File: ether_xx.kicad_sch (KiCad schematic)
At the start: 17 parts, among them J1 RJ45_LED_Shielded, J2 RJ45_LED_Shielded, U2 LAN8710A, U3 LAN8710A

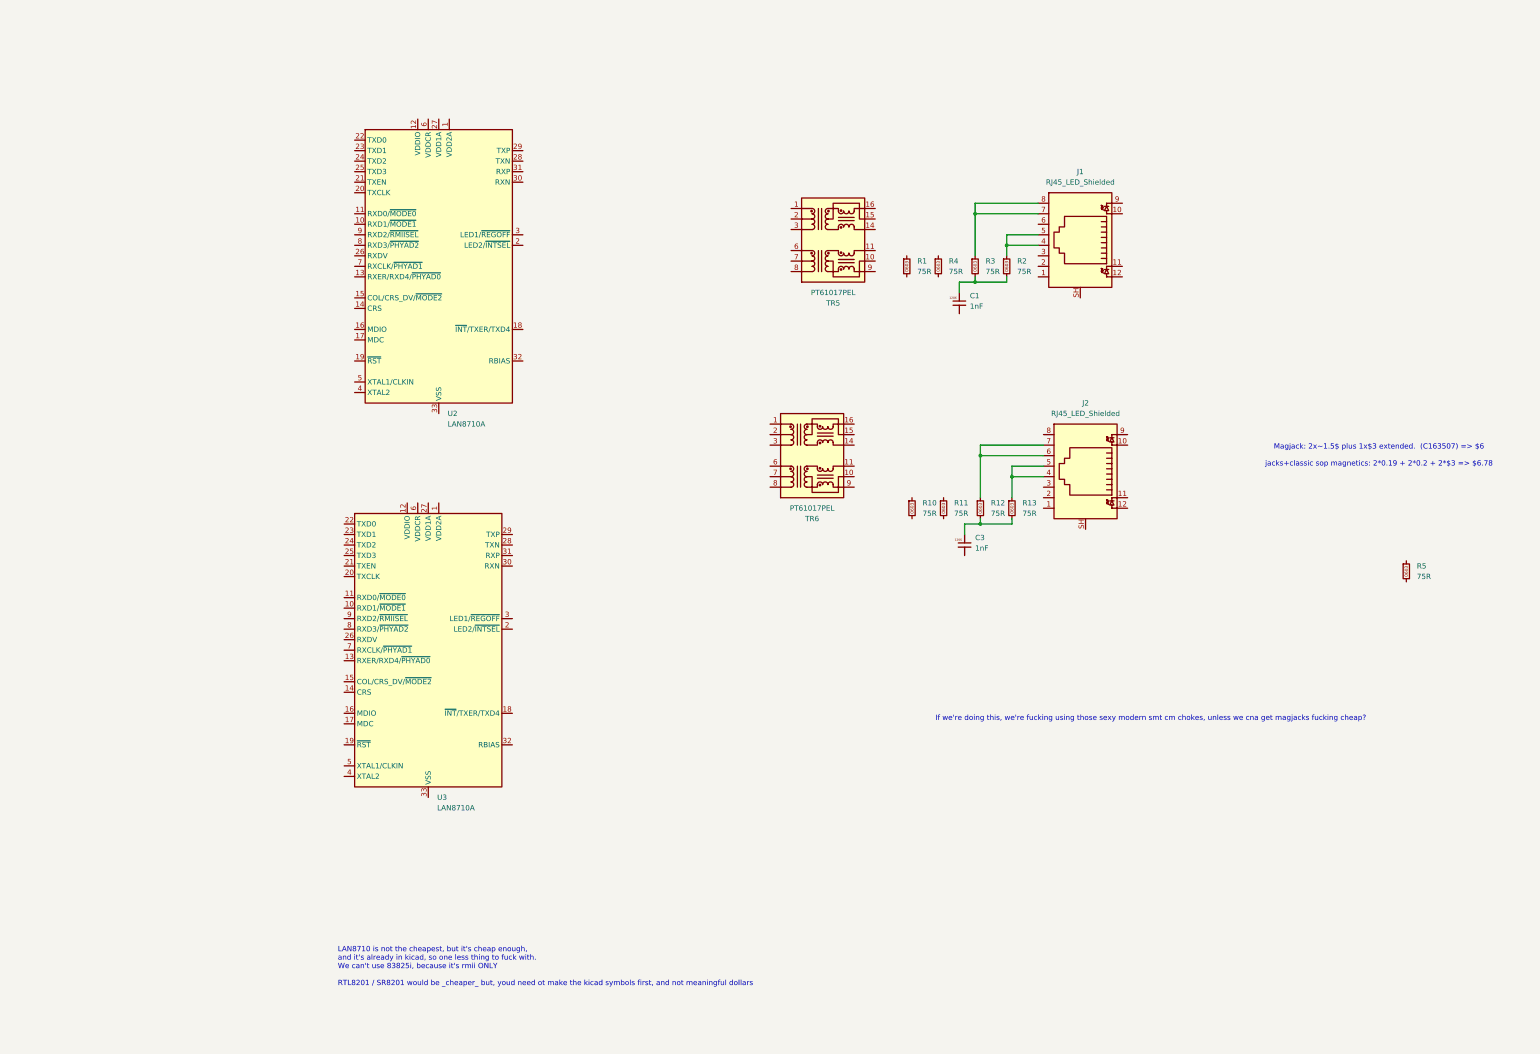
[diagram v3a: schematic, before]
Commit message: ether: switch phys, confirm magnetics, start wiring
Moved from LAN8710 to RTL8201 for the phys.  voltage mode instead of
current mode so less hassle getting them up, and less parts.  Also
cheaper, and realllly well supported too, so, all good.  Had to make a
symbol, but that's not realllly a big deal right?

We've locked in the arrangement and footprint for the magnetics now too
at least, after our research tear on them.

We've mostly figured out heirarchical bus symbols too I think...
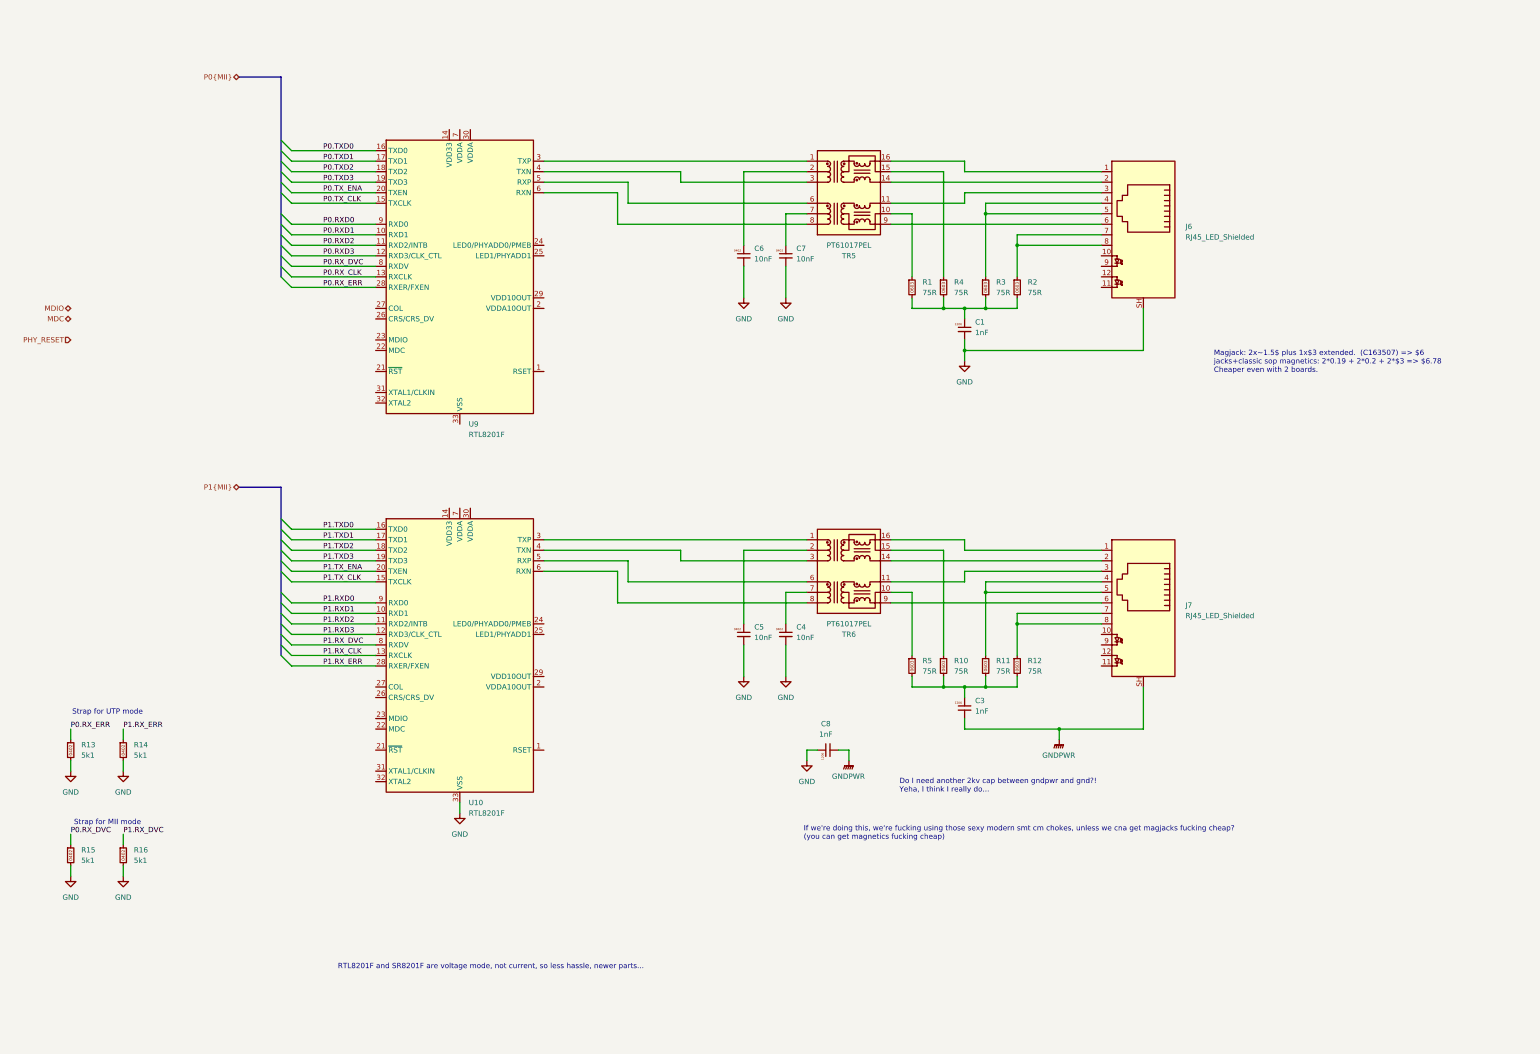
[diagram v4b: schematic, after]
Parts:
- removed J1, J2: RJ45_LED_Shielded, Connector_RJ:RJ45_Amphenol_RJHSE538X, symbol Connector:RJ45_LED_Shielded
- removed R13: 75R, Resistor_SMD:R_0603_1608Metric, symbol karl-atomic-basic:KR0603_75R
- removed U2, U3: LAN8710A, Package_DFN_QFN:QFN-32-1EP_5x5mm_P0.5mm_EP3.3x3.3mm_ThermalVias, symbol Interface_Ethernet:LAN8710A
- added C4, C5, C6, C7: 10nF, Capacitor_SMD:C_0402_1005Metric, symbol karl-atomic-basic:KC0402_10nF_50V
- added C8: 1nF, Capacitor_SMD:C_1206_3216Metric, symbol karl-atomic-basic:KC1206_1nF_2kV
- added J6, J7: RJ45_LED_Shielded, symbol karl-parts:RJ45_LED_Shielded
- added R13, R14, R15, R16: 5k1, Resistor_SMD:R_0402_1005Metric, symbol karl-atomic-basic:KR0402_5k1
- added U10, U9: RTL8201F, Package_DFN_QFN:QFN-32-1EP_5x5mm_P0.5mm_EP3.3x3.3mm_ThermalVias, symbol karl-parts:RTL8201F
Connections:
- net at C3.1, R12.2: now also R10.2, R11.2, R5.2
- net GNDPWR: now reaches C3.2
- net GNDPWR: now also C8.2, J7.SH
- net at R1.1: now also TR5.10 (C_RX)
- net at R1.2: now also C1.1, R2.2, R3.2, R4.2
- net at R10.1: now also TR6.15 (C_TX)
- net at TR5.1 (TD+): now also U9.3 (TXP)
- net at TR5.11 (RX+): now also J6.3
- net at TR5.14 (TX-): now also J6.2
- net at TR5.15 (C_TX): now also R4.1
- net at TR5.16 (TX+): now also J6.1
- net at TR5.2 (C_TD): now also C6.1
- net at TR5.3 (TD-): now also U9.4 (TXN)
- net at TR5.6 (RD+): now also U9.5 (RXP)
- net at TR5.7 (C_RD): now also C7.1
- net at TR5.8 (RD-): now also U9.6 (RXN)
- net at TR5.9 (RX-): now also J6.6
- net GND: now reaches C1.2
- net GND: now also C4.2, C5.2, C6.2, C7.2, C8.1, J6.SH, R13.2, R14.2, R15.2, R16.2, U10.33 (VSS)
- net at TR6.1 (TD+): now also U10.3 (TXP)
- net at TR6.10 (C_RX): now also R5.1
- net at TR6.11 (RX+): now also J7.3
- net at TR6.14 (TX-): now also J7.2
- net at TR6.16 (TX+): now also J7.1
- net at TR6.2 (C_TD): now also C5.1
- net at TR6.3 (TD-): now also U10.4 (TXN)
- net at TR6.6 (RD+): now also U10.5 (RXP)
- net at TR6.7 (C_RD): now also C4.1
- net at TR6.8 (RD-): now also U10.6 (RXN)
- net at TR6.9 (RX-): now also J7.6
- net at R2.1: now also J6.7, J6.8
- net at R3.1: now also J6.4, J6.5
- net at R12.1: now also J7.7, J7.8
- net at R11.1: now also J7.4, J7.5
- new net P0.RXD0: U9.9 (RXD0)
- new net P0.RXD1: U9.10 (RXD1)
- new net P0.RXD2: U9.11 (RXD2/INTB)
- new net P0.RXD3: U9.12 (RXD3/CLK_CTL)
- new net P0.RX_CLK: U9.13 (RXCLK)
- new net P0.RX_DVC: R15.1, U9.8 (RXDV)
- new net P0.RX_ERR: R13.1, U9.28 (RXER/FXEN)
- new net P0.TXD0: U9.16 (TXD0)
- new net P0.TXD1: U9.17 (TXD1)
- new net P0.TXD2: U9.18 (TXD2)
- new net P0.TXD3: U9.19 (TXD3)
- new net P0.TX_CLK: U9.15 (TXCLK)
- new net P0.TX_ENA: U9.20 (TXEN)
- new net P1.RXD0: U10.9 (RXD0)
- new net P1.RXD1: U10.10 (RXD1)
- new net P1.RXD2: U10.11 (RXD2/INTB)
- new net P1.RXD3: U10.12 (RXD3/CLK_CTL)
- new net P1.RX_CLK: U10.13 (RXCLK)
- new net P1.RX_DVC: R16.1, U10.8 (RXDV)
- new net P1.RX_ERR: R14.1, U10.28 (RXER/FXEN)
- new net P1.TXD0: U10.16 (TXD0)
- new net P1.TXD1: U10.17 (TXD1)
- new net P1.TXD2: U10.18 (TXD2)
- new net P1.TXD3: U10.19 (TXD3)
- new net P1.TX_CLK: U10.15 (TXCLK)
- new net P1.TX_ENA: U10.20 (TXEN)
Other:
- note added: "Do I need another 2kv cap between gndpwr and gnd?! Yeha, I think I really do..."
- note added: "If we're doing this, we're fucking using those sexy modern smt cm chokes, unless we cna get magjacks fucking cheap? (you can get magnetics fucking cheap)"
- note added: "Magjack: 2x~1.5$ plus 1x$3 extended. (C163507) => $6 jacks+classic sop magnetics: 2*0.19 + 2*0.2 + 2*$3 => $6.78 Cheaper even with 2 boards."
- note added: "RTL8201F and SR8201F are voltage mode, not current, so less hassle, newer parts..."
- note added: "Strap for MII mode"
- note added: "Strap for UTP mode"
- note removed: "If we're doing this, we're fucking using those sexy modern smt cm chokes, unless we cna get magjacks fucking cheap?"
- note removed: "LAN8710 is not the cheapest, but it's cheap enough, and it's already in kicad, so one less thing to fuck with. We can't use 83825i, because it's rmii ONLY RTL8201 / SR8201 would be _cheaper_ but, youd need ot make the kicad symbols first, and not meaningful dollars"
- note removed: "Magjack: 2x~1.5$ plus 1x$3 extended. (C163507) => $6 jacks+classic sop magnetics: 2*0.19 + 2*0.2 + 2*$3 => $6.78"
- moved on the sheet: C1, R1, R2, R3, R4, TR5

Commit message: continue with the phys, add debug, hook more up
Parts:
- added C11, C12, C13, C14: 100nF, Capacitor_SMD:C_0402_1005Metric, symbol karl-atomic-basic:KC0402_100nF
- added R21, R23, R27, R28: 510R, Resistor_SMD:R_0603_1608Metric, symbol karl-atomic-basic:KR0603_510R
- added R22, R24, R25, R26: 5k1, Resistor_SMD:R_0402_1005Metric, symbol karl-atomic-basic:KR0402_5k1
- added R29, R30: 2.49k, Resistor_SMD:R_0402_1005Metric, symbol karl-atomic-basic:KR0402_2k49
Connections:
- net GND: now also J6.11, J6.9, J7.10, J7.11, U10.31 (XTAL1), U9.31 (XTAL1), U9.33 (VSS), C11.2, C12.2, C13.2, C14.2, R22.2, R25.1, R26.2, R29.2, R30.2
- net PHY_RESET: now also U10.21 (~{RST}), U9.21 (~{RST})
- net P0.LED0: now reaches J6.10
- net P0.LED1: now reaches J6.12
- net at U9.1 (RSET): now also R29.1
- net at U9.2 (VDDA10OUT): now also C11.1
- net at U9.24 (LED0/PHYADD0/PMEB): now also R25.2, R27.1
- net at U9.25 (LED1/PHYADD1): now also R26.1, R28.1
- net at U9.29 (VDD10OUT): now also C12.1
- net PHY_25M_IN: now reaches U9.32 (XTAL2/CLKIN)
- net PHY_25M_IN: now also U10.32 (XTAL2/CLKIN)
- net P1.LED1: now reaches J7.12
- net P1.LED1: now also R23.2, R28.2
- net P1.LED0: now reaches J7.9
- net P1.LED0: now also R21.2, R27.2
- net at U10.1 (RSET): now also R30.1
- net at U10.2 (VDDA10OUT): now also C13.1
- net at U10.24 (LED0/PHYADD0/PMEB): now also R21.1, R24.2
- net at U10.25 (LED1/PHYADD1): now also R22.1, R23.1
- net at U10.29 (VDD10OUT): now also C14.1
- new net +3V3: R24.1
- no-connect marks 0 -> 4
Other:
- note added: "PHYADDR: 00"
- note added: "PHYADDR: 01"

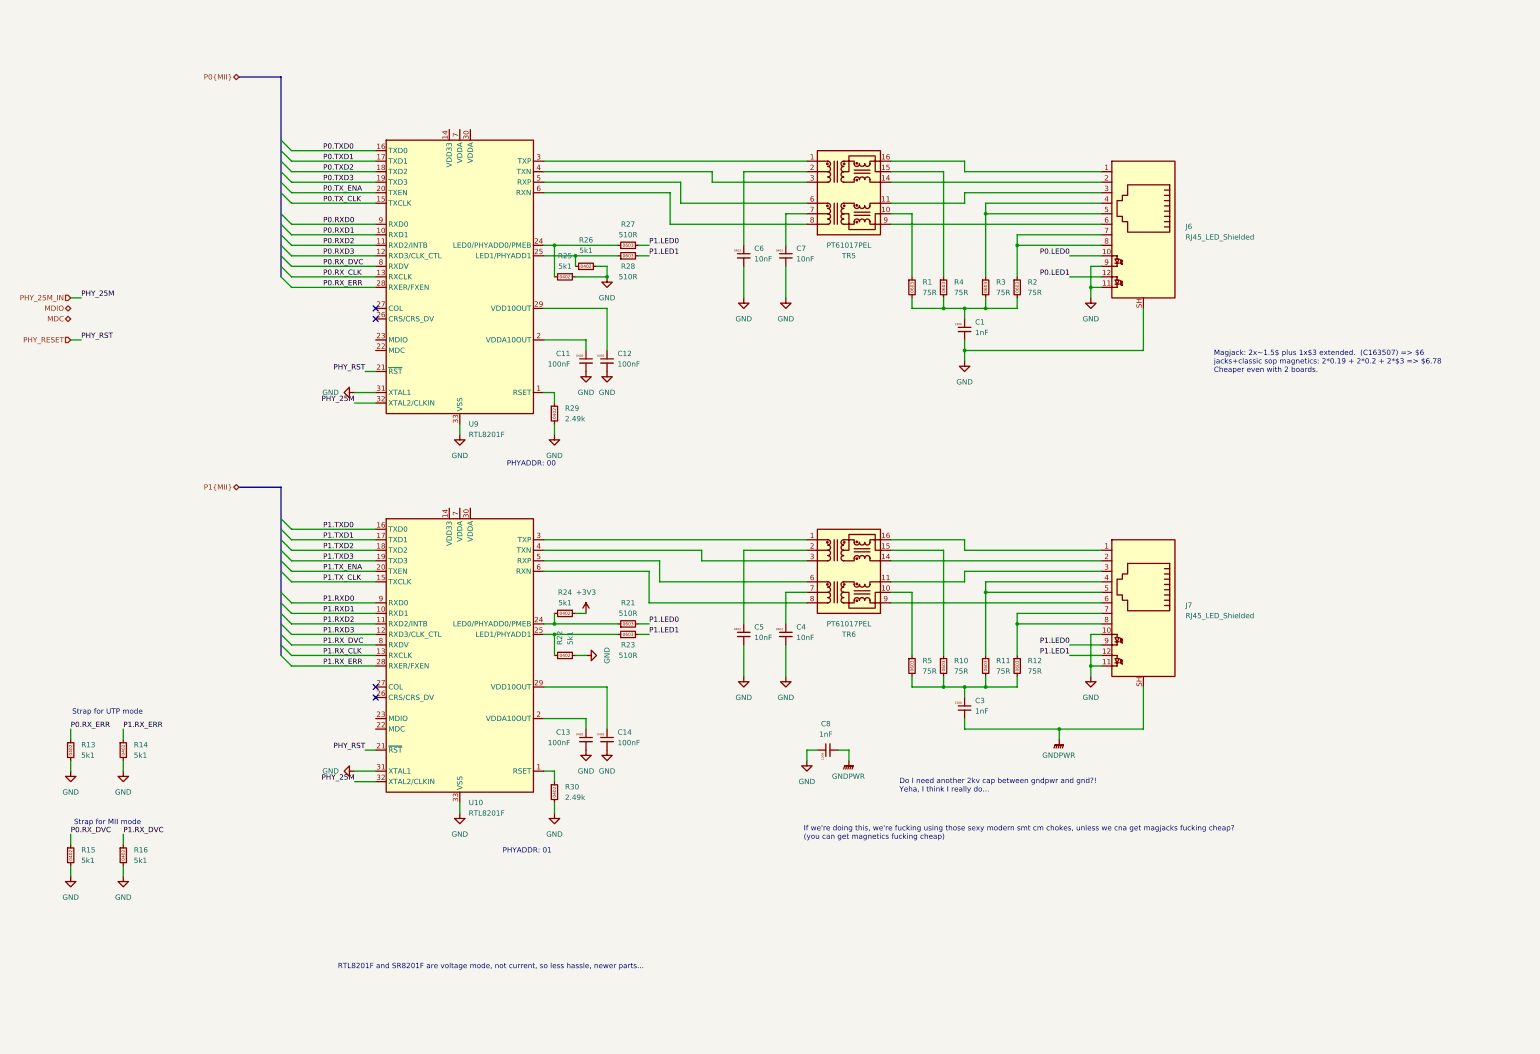
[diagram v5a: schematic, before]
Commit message: push forwards: clock muxing, filling in blanks
Finished off the ethernet section finally.
Sorted a solution to the 25M phy clocks required for ethercat
Connected CAN as per existing hardware (and fixed a bug in speed mode)
Sorted out bypassing for MCU
Added more thoughts on the external interfaces
Started on a 24V supply
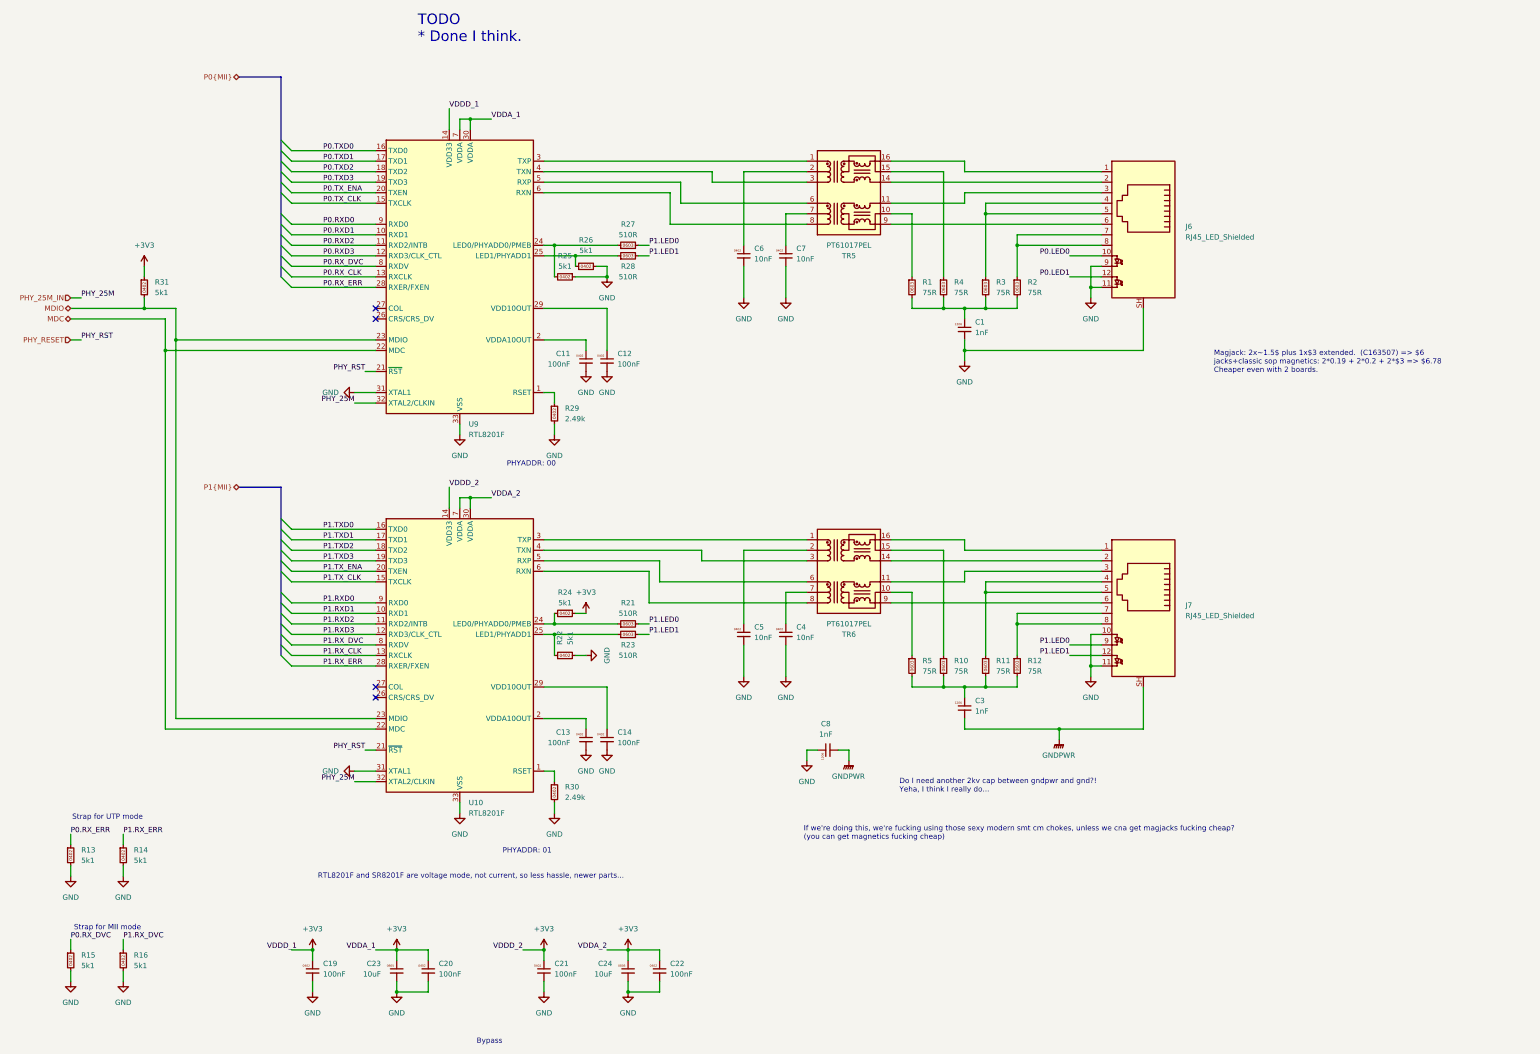
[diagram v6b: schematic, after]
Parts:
- added C19, C20, C21, C22: 100nF, Capacitor_SMD:C_0402_1005Metric, symbol karl-atomic-basic:KC0402_100nF
- added C23, C24: 10uF, Capacitor_SMD:C_0805_2012Metric, symbol karl-atomic-basic:KC0805_10uF_25V
- added R31: 5k1, Resistor_SMD:R_0402_1005Metric, symbol karl-atomic-basic:KR0402_5k1
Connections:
- net +3V3: now also U10.14 (VDD33), U10.30 (VDDA), U10.7 (VDDA), U9.14 (VDD33), U9.30 (VDDA), U9.7 (VDDA), C19.1, C20.1, C21.1, C22.1, C23.1, C24.1, R31.1
- net GND: now also C19.2, C20.2, C21.2, C22.2, C23.2, C24.2
- net MDC: now also U10.22 (MDC), U9.22 (MDC)
- net MDIO: now also U10.23 (MDIO), U9.23 (MDIO), R31.2
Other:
- note added: "Bypass"
- note added: "TODO * Done I think."
- moved on the sheet: R13, R14, R15, R16

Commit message: finish a 24V supply
went with a more modern one, plenty of room.  Should be pretty good now.
Went over and filled in a bunch of missing parts and things, cleaned up
as much as I could 0603 vs 0402 for most, updated some thigns to current
atomic part library.

still to go, the "pi" interface and some sort of spi/io interface?
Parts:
- J6, J7: footprint (none) -> Connector_RJ:RJ45_Amphenol_RJHSE538X; LCSC Part # (none) -> C7501824; MPN (none) -> HC-WK88-H16-DB; jlcbasic (none) -> 0
